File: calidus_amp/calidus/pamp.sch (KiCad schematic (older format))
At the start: 48 parts, among them U1 TDA7293, U2 TDA7293

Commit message: Upgraded power supply
Using new power supply design with 3pin linear regulator
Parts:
- U1, U2: symbol tda7293:TDA7293 -> calidus-rescue:TDA7293-tda7293
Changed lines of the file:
@@
 $EndDescr
 $Comp
-L tda7293:TDA7293 U1
+L calidus-rescue:TDA7293-tda7293 U1
 U 1 1 5C37C649
 P 3900 2500
+AR Path="/5C37C649" Ref="U1"  Part="1"
+AR Path="/5C37BC7C/5C37C649" Ref="U1"  Part="1"
 F 0 "U1" H 4341 2546 50  0000 L CNN
 F 1 "TDA7293" H 4341 2455 50  0000 L CNN
@@
 -pwvs
 $Comp
-L tda7293:TDA7293 U2
+L calidus-rescue:TDA7293-tda7293 U2
 U 1 1 5C38B287
 P 3900 5900
+AR Path="/5C38B287" Ref="U2"  Part="1"
+AR Path="/5C37BC7C/5C38B287" Ref="U2"  Part="1"
 F 0 "U2" H 4341 5946 50  0000 L CNN
 F 1 "TDA7293" H 4341 5855 50  0000 L CNN

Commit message: Update of the schematic
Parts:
- removed C10, C11, C12, C15, C16, C17, C18, C19, C20, C21, C22: 100n, symbol Device:C
- removed C14: 10u, symbol Device:CP
- removed C2, C3, C4: 220u, symbol Device:CP
- removed C6: 3p3, symbol Device:C
- removed C8: 47u, symbol Device:CP
- removed D5: 1n4148, symbol Device:D
- removed R10, R11, R12: 3.9, symbol Device:R
- removed R14: 10, symbol Device:R
- removed R16: 30K, symbol Device:R
- removed R17: 20K, symbol Device:R
- removed R2, R3, R4: 200, symbol Device:R
- removed R5, R6, R7: 5k1, symbol Device:R
- added C? (x3): 220u, symbol Device:CP
- added C?: 47u, symbol Device:CP
- added C?: 10u, symbol Device:CP
- added C? (x11): 100n, symbol Device:C
- added C?: 3p3, symbol Device:C
- added R? (x3): 200, symbol Device:R
- added R? (x3): 5k1, symbol Device:R
- added R? (x3): 3.9, symbol Device:R
- added R?: 10, symbol Device:R
- added R?: 20k, symbol Device:R
- C15: renamed from C13; Voltage (none) -> 16V
- C21: renamed from C7; Voltage (none) -> 35V
- C22: renamed from C1; Voltage (none) -> 35V
- C24: renamed from C5; Type (none) -> NP0; Voltage (none) -> 100V
- C25: renamed from C9; Type (none) -> PP; Voltage (none) -> 63V
- D13: renamed from D1; value 1n5404 -> 1N5404
- D14: renamed from D2; value 1n5404 -> 1N5404
- D15: renamed from D3; value 1n5404 -> 1N5404
- D16: renamed from D4; value 1n5404 -> 1N5404
- R14: renamed from R15; value 10K -> 20k; Power (none) -> 1/4; Type (none) -> C
- R18: renamed from R1; Power (none) -> 1/4; Type (none) -> MF
- R22: renamed from R9; Type (none) -> C
- R23: renamed from R13; Type (none) -> C
- R28: renamed from R8; Type (none) -> MF
- renumbered U1 to U3, U2 to U4
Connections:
- net labels added: GNDD, stby
- net labels removed: GNDA
- wire segments 162 -> 154

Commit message: Daily update
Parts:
- removed R28, R? (x2): 5k1, symbol Device:R
- removed R? (x3): 200, symbol Device:R
- added R? (x3): 499, symbol Device:R
- added R? (x3): 13k3, symbol Device:R
- R18: value 200 -> 499
- R?: value 5k1 -> 13k3
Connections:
- net GNDS: now also R?.1
- net at C24.1, D13.2 (A), D14.1 (K)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: now also R?.1
- net at C24.2, U3.2 (-): now also R?.1, R?.2
- net at C?.1, D15.2 (A), D16.1 (K)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: now also R?.1
- net at C?.2, U4.2 (-): now also R?.1, R?.2
- net at U4.3 (+): now also R?.1, R?.2
- net at C?.1: now also R?.2 (x3)
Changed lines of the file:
@@
 P 2650 2400
 F 0 "R18" V 2261 2400 50  0000 C CNN
-F 1 "200" V 2352 2400 50  0000 C CNN
+F 1 "499" V 2352 2400 50  0000 C CNN
 F 2 "" V 2580 2400 50  0001 C CNN
 F 3 "~" H 2650 2400 50  0001 C CNN
@@
 Wire Wire Line
 	2900 6600 3000 6600
-$Comp
-L Device:R R28
-U 1 1 5C38B292
-P 3150 6600
-F 0 "R28" V 2761 6600 50  0000 C CNN
-F 1 "5k1" V 2852 6600 50  0000 C CNN
-F 2 "" V 3080 6600 50  0001 C CNN
-F 3 "~" H 3150 6600 50  0001 C CNN
-F 4 "1/2" V 2943 6600 50  0000 C CNN "Power"
-F 5 "MF" V 3034 6600 50  0000 C CNN "Type"
-	1    3150 6600
-	0    1    1    0
-$EndComp
 Wire Wire Line
 	3300 6600 3400 6600
@@
 $EndComp
 $Comp
-L Device:R R?
-U 1 1 5C467D6D
-P 2650 2600
-F 0 "R?" V 2765 2600 50  0000 C CNN
-F 1 "200" V 2856 2600 50  0000 C CNN
-F 2 "" V 2580 2600 50  0001 C CNN
-F 3 "~" H 2650 2600 50  0001 C CNN
-F 4 "1/4" V 2947 2600 50  0000 C CNN "Power"
-F 5 "MF" V 3038 2600 50  0000 C CNN "Type"
-	1    2650 2600
-	0    1    1    0
-$EndComp
-$Comp
-L Device:R R?
-U 1 1 5C467F48
-P 2650 5800
-F 0 "R?" V 2261 5800 50  0000 C CNN
-F 1 "200" V 2352 5800 50  0000 C CNN
-F 2 "" V 2580 5800 50  0001 C CNN
-F 3 "~" H 2650 5800 50  0001 C CNN
-F 4 "1/4" V 2443 5800 50  0000 C CNN "Power"
-F 5 "MF" V 2534 5800 50  0000 C CNN "Type"
-	1    2650 5800
-	0    1    1    0
-$EndComp
-$Comp
-L Device:R R?
-U 1 1 5C46800E
-P 2650 6000
-F 0 "R?" V 2765 6000 50  0000 C CNN
-F 1 "200" V 2856 6000 50  0000 C CNN
-F 2 "" V 2580 6000 50  0001 C CNN
-F 3 "~" H 2650 6000 50  0001 C CNN
-F 4 "1/4" V 2947 6000 50  0000 C CNN "Power"
-F 5 "MF" V 3038 6000 50  0000 C CNN "Type"
-	1    2650 6000
-	0    1    1    0
-$EndComp
-$Comp
 L Device:CP C?
 U 1 1 5C4684D2
@@
 $Comp
 L Device:R R?
-U 1 1 5C46954A
-P 3150 5200
-F 0 "R?" V 2761 5200 50  0000 C CNN
-F 1 "5k1" V 2852 5200 50  0000 C CNN
-F 2 "" V 3080 5200 50  0001 C CNN
-F 3 "~" H 3150 5200 50  0001 C CNN
-F 4 "1/2" V 2943 5200 50  0000 C CNN "Power"
-F 5 "MF" V 3034 5200 50  0000 C CNN "Type"
-	1    3150 5200
-	0    1    1    0
-$EndComp
-$Comp
-L Device:R R?
-U 1 1 5C4696A1
-P 3150 3200
-F 0 "R?" V 2761 3200 50  0000 C CNN
-F 1 "5k1" V 2852 3200 50  0000 C CNN
-F 2 "" V 3080 3200 50  0001 C CNN
-F 3 "~" H 3150 3200 50  0001 C CNN
-F 4 "1/2" V 2943 3200 50  0000 C CNN "Power"
-F 5 "MF" V 3034 3200 50  0000 C CNN "Type"
-	1    3150 3200
-	0    1    1    0
-$EndComp
-$Comp
-L Device:R R?
 U 1 1 5C469739
 P 3150 1800
 F 0 "R?" V 2761 1800 50  0000 C CNN
-F 1 "5k1" V 2852 1800 50  0000 C CNN
+F 1 "13k3" V 2852 1800 50  0000 C CNN
 F 2 "" V 3080 1800 50  0001 C CNN
 F 3 "~" H 3150 1800 50  0001 C CNN
@@
 Text HLabel 7400 1300 2    50   Input ~ 0
 stby
+$Comp
+L Device:R R?
+U 1 1 5C483CBD
+P 2650 2600
+F 0 "R?" V 2765 2600 50  0000 C CNN
+F 1 "499" V 2856 2600 50  0000 C CNN
+F 2 "" V 2580 2600 50  0001 C CNN
+F 3 "~" H 2650 2600 50  0001 C CNN
+F 4 "1/4" V 2947 2600 50  0000 C CNN "Power"
+F 5 "MF" V 3038 2600 50  0000 C CNN "Type"
+	1    2650 2600
+	0    1    1    0
+$EndComp
+$Comp
+L Device:R R?
+U 1 1 5C483D2D
+P 2650 5800
+F 0 "R?" V 2261 5800 50  0000 C CNN
+F 1 "499" V 2352 5800 50  0000 C CNN
+F 2 "" V 2580 5800 50  0001 C CNN
+F 3 "~" H 2650 5800 50  0001 C CNN
+F 4 "1/4" V 2443 5800 50  0000 C CNN "Power"
+F 5 "MF" V 2534 5800 50  0000 C CNN "Type"
+	1    2650 5800
+	0    1    1    0
+$EndComp
+$Comp
+L Device:R R?
+U 1 1 5C483DC7
+P 2650 6000
+F 0 "R?" V 2765 6000 50  0000 C CNN
+F 1 "499" V 2856 6000 50  0000 C CNN
+F 2 "" V 2580 6000 50  0001 C CNN
+F 3 "~" H 2650 6000 50  0001 C CNN
+F 4 "1/4" V 2947 6000 50  0000 C CNN "Power"
+F 5 "MF" V 3038 6000 50  0000 C CNN "Type"
+	1    2650 6000
+	0    1    1    0
+$EndComp
+$Comp
+L Device:R R?
+U 1 1 5C4843CA
+P 3150 3200
+F 0 "R?" V 2761 3200 50  0000 C CNN
+F 1 "13k3" V 2852 3200 50  0000 C CNN
+F 2 "" V 3080 3200 50  0001 C CNN
+F 3 "~" H 3150 3200 50  0001 C CNN
+F 4 "1/2" V 2943 3200 50  0000 C CNN "Power"
+F 5 "MF" V 3034 3200 50  0000 C CNN "Type"
+	1    3150 3200
+	0    1    1    0
+$EndComp
+$Comp
+L Device:R R?
+U 1 1 5C484452
+P 3150 5200
+F 0 "R?" V 2761 5200 50  0000 C CNN
+F 1 "13k3" V 2852 5200 50  0000 C CNN
+F 2 "" V 3080 5200 50  0001 C CNN
+F 3 "~" H 3150 5200 50  0001 C CNN
+F 4 "1/2" V 2943 5200 50  0000 C CNN "Power"
+F 5 "MF" V 3034 5200 50  0000 C CNN "Type"
+	1    3150 5200
+	0    1    1    0
+$EndComp
+$Comp
+L Device:R R?
+U 1 1 5C4844EE
+P 3150 6600
+F 0 "R?" V 2761 6600 50  0000 C CNN
+F 1 "13k3" V 2852 6600 50  0000 C CNN
+F 2 "" V 3080 6600 50  0001 C CNN
+F 3 "~" H 3150 6600 50  0001 C CNN
+F 4 "1/2" V 2943 6600 50  0000 C CNN "Power"
+F 5 "MF" V 3034 6600 50  0000 C CNN "Type"
+	1    3150 6600
+	0    1    1    0
+$EndComp
 $EndSCHEMATC

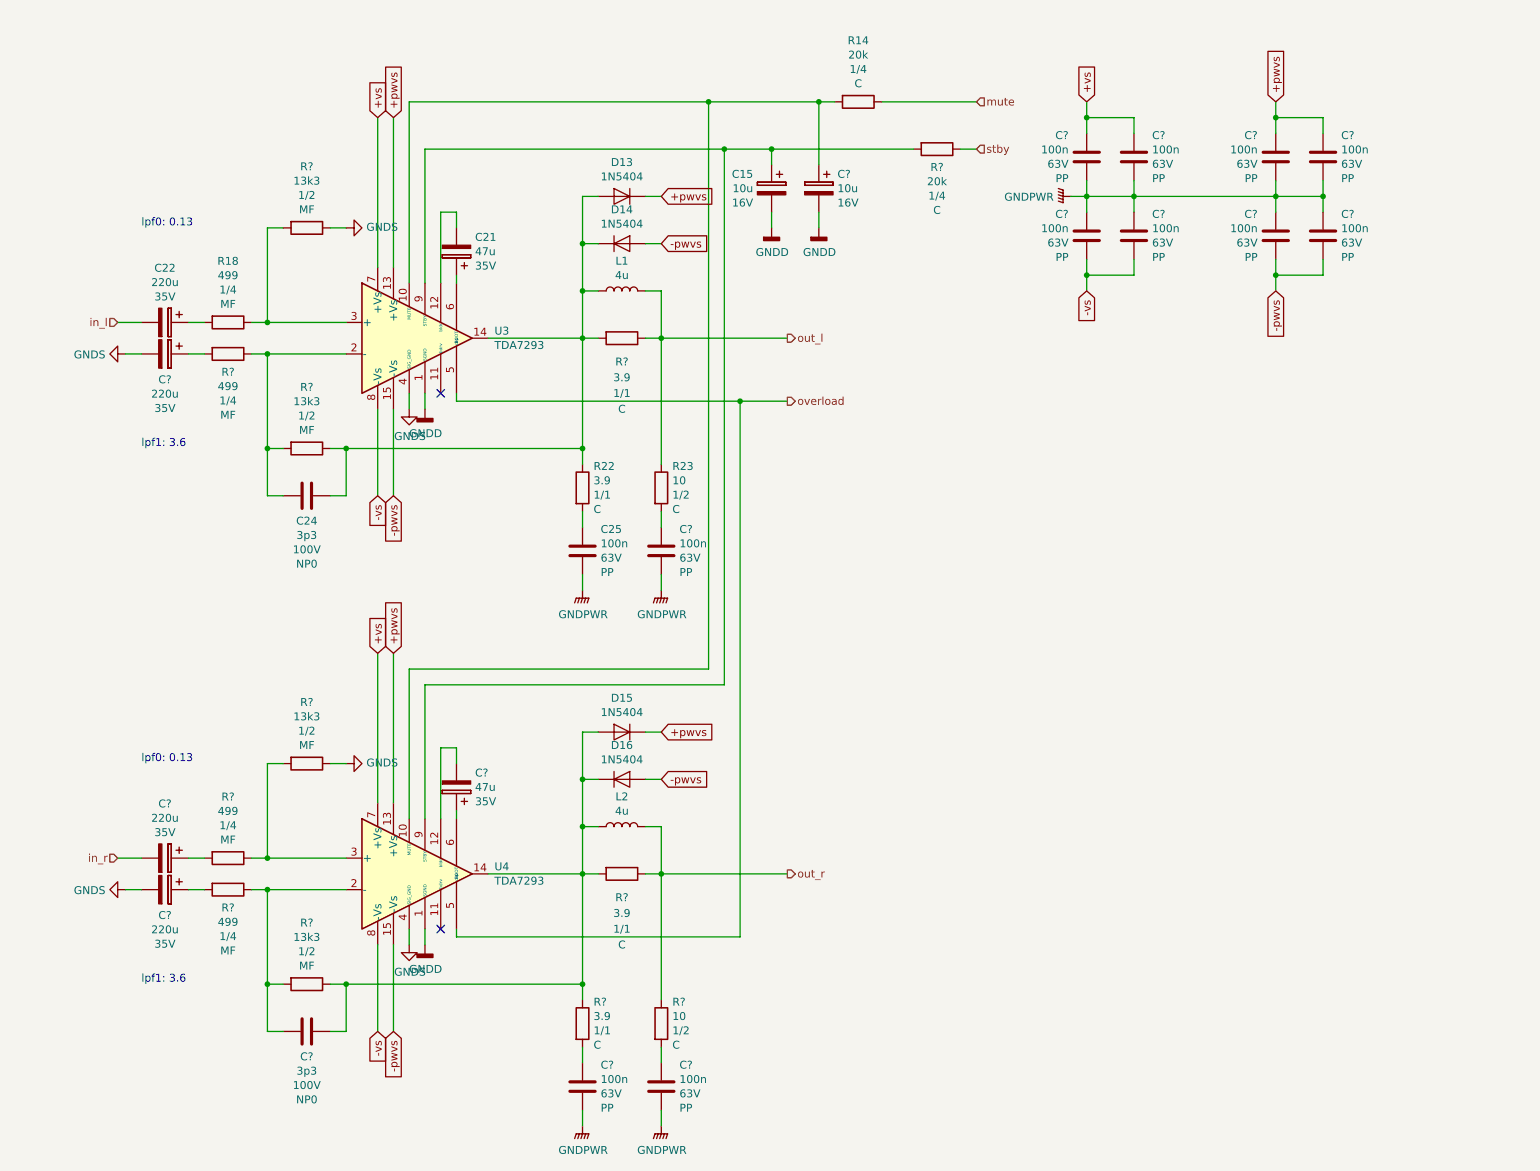
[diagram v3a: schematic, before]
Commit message: Updated component designators and finished CMU
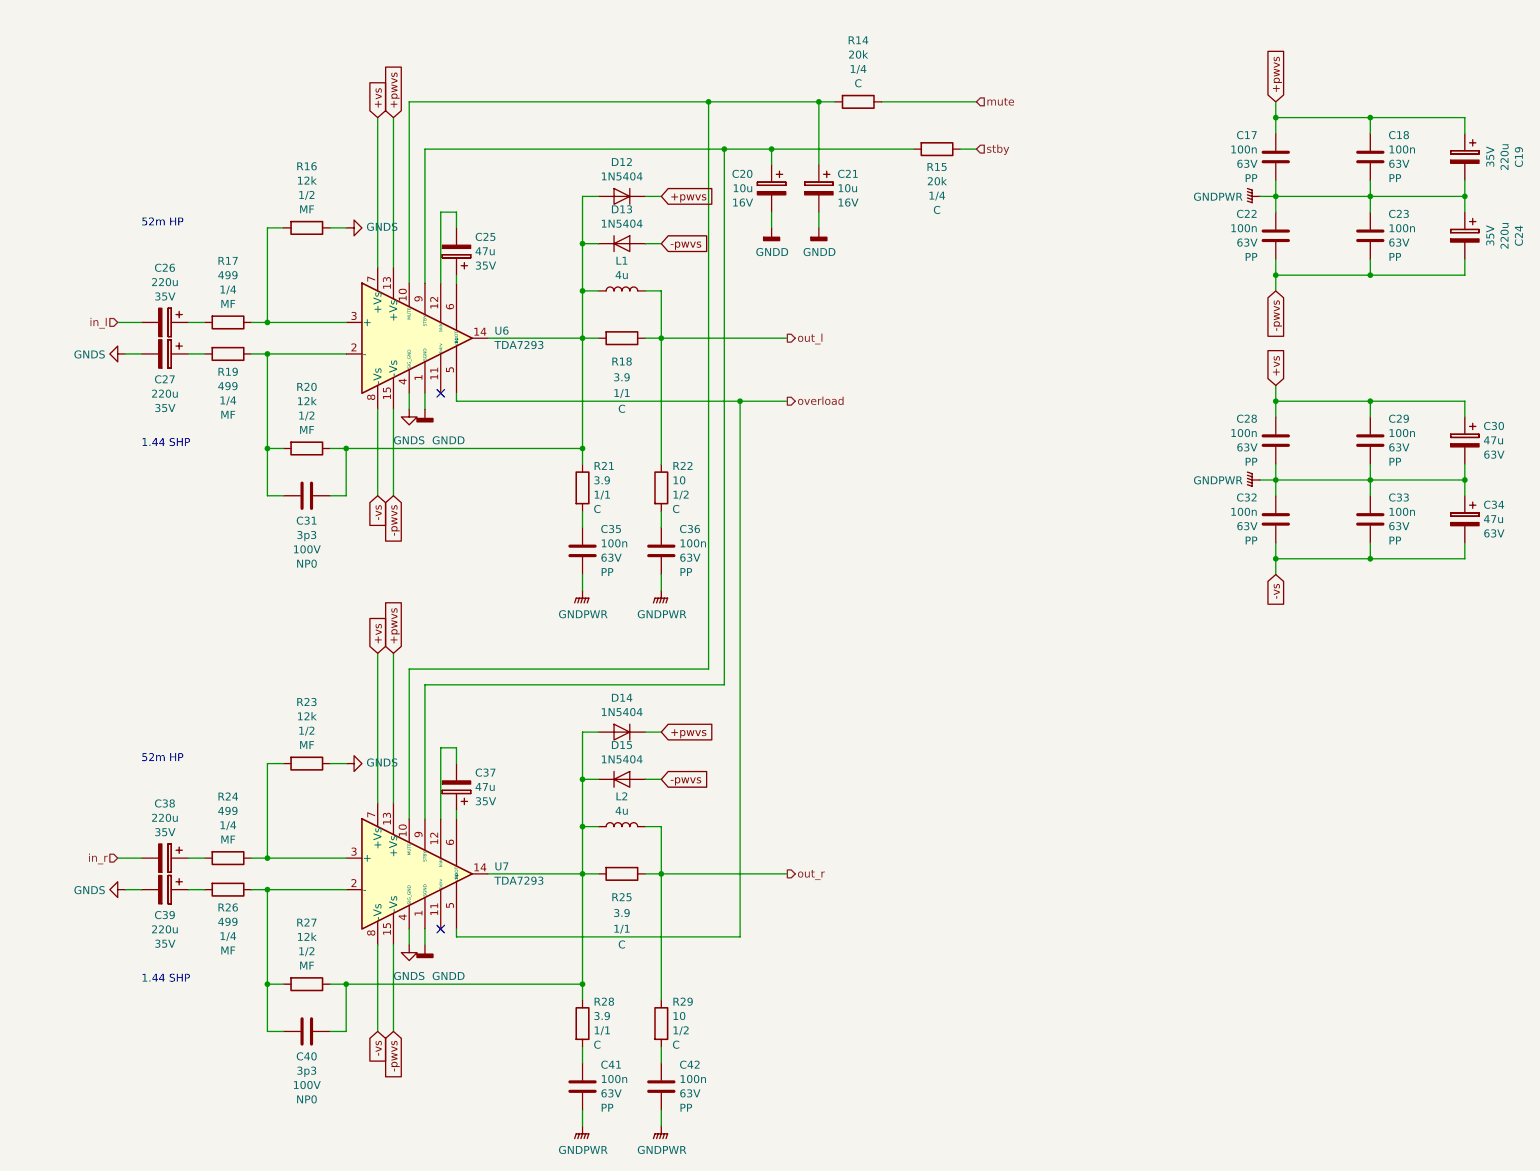
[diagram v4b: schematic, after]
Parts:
- added C19, C24: 220u, symbol Device:CP
- added C30, C34: 47u, symbol Device:CP
- R16, R20, R23, R27: renamed from R?; value 13k3 -> 12k
- gave numbers to parts that had none: 25
- renumbered C15 to C20, C21 to C25, C22 to C26, C24 to C31, C25 to C35, D13 to D12, D14 to D13, D15 to D14, D16 to D15, R18 to R17, R22 to R21, R23 to R22, U3 to U6, U4 to U7
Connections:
- net +pwvs: now also C19.1
- net +vs: now also C30.1
- net -pwvs: now also C24.2
- net -vs: now also C34.2
- net GNDPWR: now also C19.2, C24.1, C30.2, C34.1
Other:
- note added: "1.44 SHP"
- note added: "52m HP"
- note removed: "lpf0: 0.13"
- note removed: "lpf1: 3.6"
- moved on the sheet: C18, C23, C28, C29, C32, C33
